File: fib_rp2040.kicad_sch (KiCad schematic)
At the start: 0 parts

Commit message: added several ICs, implementted schematics for charger, boost converter and LDOs
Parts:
- added U3: rpi_pico, Fibel2:rpi_pico, symbol Fibel2:rpi_pico
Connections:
- new net: U3.13 (GND), U3.18 (GND), U3.23 (GND), U3.28 (GND), U3.3 (GND), U3.38 (GND), U3.8 (GND), U3.D2 (GND)
- new net: U3.A (USB_SHIELD), U3.B (USB_SHIELD), U3.C (USB_SHIELD), U3.D (USB_SHIELD)
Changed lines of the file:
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@@
 	(generator_version "8.0")
 	(paper "A4")
+	(symbol
+		(lib_id "Fibel2:rpi_pico")
+		(at 74.93 91.44 0)
+		(unit 1)
+		(exclude_from_sim no)
+		(in_bom yes)
+		(on_board yes)
+		(dnp no)
+		(fields_autoplaced yes)
+		(property "Reference" "U3"
+			(at 74.93 43.18 0)
+			(effects
+				(font
+					(size 1.27 1.27)
+				)
+			)
+		)
+		(property "Value" "rpi_pico"
+			(at 74.93 45.72 0)
+			(effects
+				(font
+					(size 1.27 1.27)
+				)
+			)
+		)
+		(property "Footprint" "Fibel2:rpi_pico"
+			(at 61.722 139.446 0)
+			(effects
+				(font
+					(size 1.27 1.27)
+				)
+				(justify bottom)
+				(hide yes)
+			)
+		)
+		(property "Datasheet" ""
+			(at 74.93 91.44 0)
+			(effects
+				(font
+					(size 1.27 1.27)
+				)
+				(hide yes)
+			)
+		)
+		(property "Description" ""
+			(at 74.93 91.44 0)
+			(effects
+				(font
+					(size 1.27 1.27)
+				)
+				(hide yes)
+			)
+		)
+		(property "MF" "Raspberry Pi"
+			(at 60.96 141.478 0)
+			(effects
+				(font
+					(size 1.27 1.27)
+				)
+				(justify bottom)
+				(hide yes)
+			)
+		)
+		(property "MP" "SC0915"
+			(at 58.42 143.764 0)
+			(effects
+				(font
+					(size 1.27 1.27)
+				)
+				(justify bottom)
+				(hide yes)
+			)
+		)
+		(pin "10"
+		)
+		(pin "15"
+		)
+		(pin "16"
+		)
+		(pin "37"
+		)
+		(pin "38"
+		)
+		(pin "39"
+		)
+		(pin "TP4"
+		)
+		(pin "TP5"
+		)
+		(pin "TP6"
+		)
+		(pin "30"
+		)
+		(pin "31"
+		)
+		(pin "32"
+		)
+		(pin "33"
+		)
+		(pin "13"
+		)
+		(pin "14"
+		)
+		(pin "A"
+		)
+		(pin "B"
+		)
+		(pin "C"
+		)
+		(pin "D"
+		)
+		(pin "D1"
+		)
+		(pin "7"
+		)
+		(pin "8"
+		)
+		(pin "9"
+		)
+		(pin "40"
+		)
+		(pin "5"
+		)
+		(pin "6"
+		)
+		(pin "11"
+		)
+		(pin "12"
+		)
+		(pin "26"
+		)
+		(pin "27"
+		)
+		(pin "28"
+		)
+		(pin "29"
+		)
+		(pin "3"
+		)
+		(pin "D2"
+		)
+		(pin "D3"
+		)
+		(pin "TP1"
+		)
+		(pin "TP2"
+		)
+		(pin "TP3"
+		)
+		(pin "34"
+		)
+		(pin "35"
+		)
+		(pin "36"
+		)
+		(pin "2"
+		)
+		(pin "20"
+		)
+		(pin "21"
+		)
+		(pin "22"
+		)
+		(pin "1"
+		)
+		(pin "23"
+		)
+		(pin "24"
+		)
+		(pin "25"
+		)
+		(pin "4"
+		)
+		(pin "17"
+		)
+		(pin "18"
+		)
+		(pin "19"
+		)
+		(instances
+			(project "Fibel2"
+				(path "/862c21e2-7ec9-4f80-a33c-aad02ea9423e/32a7c27a-139a-4e74-bd6e-19af0f586a3c"
+					(reference "U3")
+					(unit 1)
+				)
+			)
+		)
+	)
 )

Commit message: added symbol&footprint for orin/sodimm, added a bunch of specs and docs, partially implemented audio, full steam ahead
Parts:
- U3: footprint Fibel2:rpi_pico -> Fibel2:RPi Pico
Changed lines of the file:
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@@
 			)
 		)
-		(property "Footprint" "Fibel2:rpi_pico"
+		(property "Footprint" "Fibel2:RPi Pico"
 			(at 61.722 139.446 0)
 			(effects

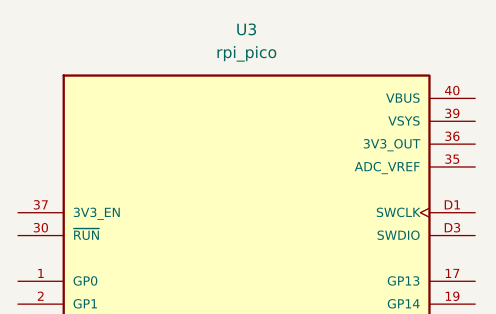
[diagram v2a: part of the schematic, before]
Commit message: added nets for 40 pin headers (epd & rpi header) connected some of the nets i'm reeusing
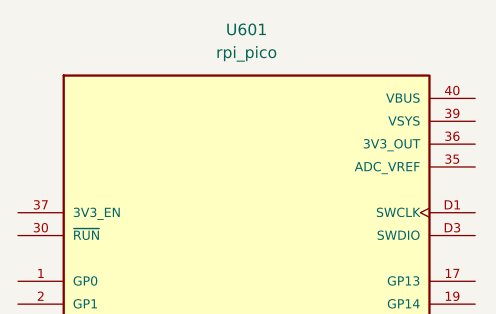
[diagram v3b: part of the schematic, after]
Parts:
- renumbered U3 to U601
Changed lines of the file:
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@@
 		(dnp no)
 		(fields_autoplaced yes)
-		(property "Reference" "U3"
+		(property "Reference" "U601"
 			(at 74.93 43.18 0)
 			(effects
@@
 			(project "Fibel2"
 				(path "/862c21e2-7ec9-4f80-a33c-aad02ea9423e/32a7c27a-139a-4e74-bd6e-19af0f586a3c"
-					(reference "U3")
+					(reference "U601")
 					(unit 1)
 				)
